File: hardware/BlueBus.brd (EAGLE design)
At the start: 70 x 45 mm, 77 parts

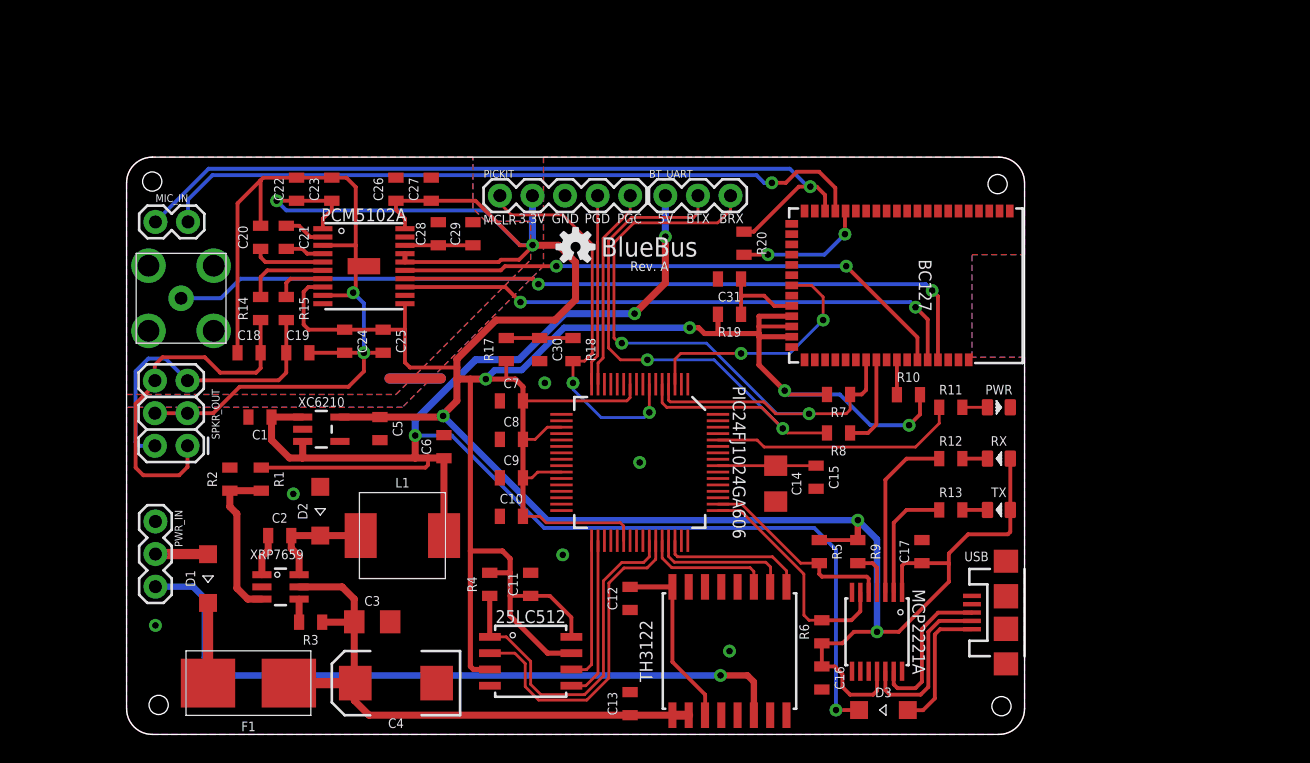
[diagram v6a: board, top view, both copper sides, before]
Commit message: [IMP] hardware: MIC IN Fixes
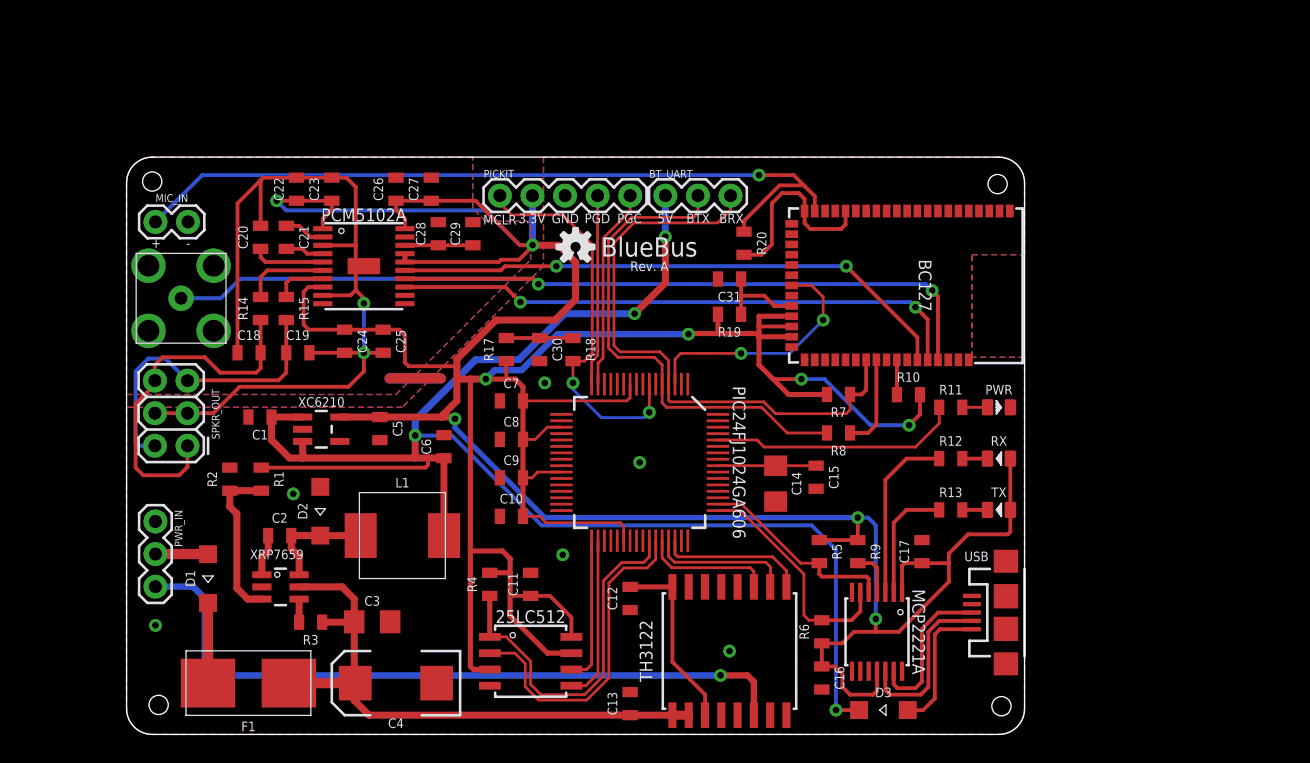
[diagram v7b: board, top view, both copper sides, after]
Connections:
- removed net BT_MIC_BIAS: BC127.17, R20.2
- removed net BT_MIC_RN: BC127.18, MIC_IN.2
- removed net BT_MIC_RP: BC127.19, MIC_IN.1, R20.1
- new net BT_MIC_IN: BC127.20, MIC_IN.1, R20.1
- new net MIC_BIAS: BC127.17, BC127.21, R20.2
- net 3.3V: no longer PCM5102A.11
- net GND: now also MIC_IN.2, PCM5102A.11
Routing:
- net BT_MIC_RP: track 62.6 -> 0.00 mm, vias 1 -> 0
- net BT_MIC_IN: track 0.00 -> 61.4 mm, vias 0 -> 1
- net BT_MIC_RN: track 55.9 -> 0.00 mm, vias 1 -> 0
- net MIC_BIAS: track 0.00 -> 15.3 mm
- net BT_MIC_BIAS: track 10.7 -> 0.00 mm, vias 2 -> 0
- net BT_UTX: track 57.2 -> 46.8 mm, vias 2 -> 0
- net BT_URX: track 56.4 -> 46.5 mm, vias 2 -> 0

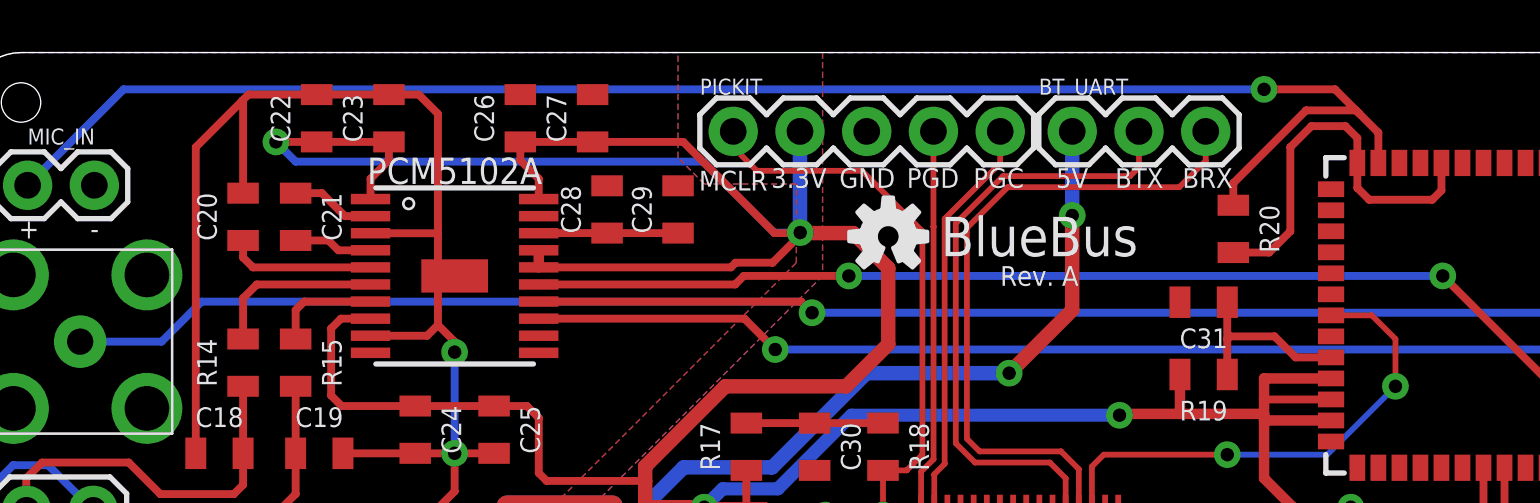
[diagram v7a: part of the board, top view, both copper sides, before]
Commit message: [IMP] hardware: Clean up traces * Clean up trace runs so we use less VIAs * Ensure that VIAs are not mid-trace on signal lines
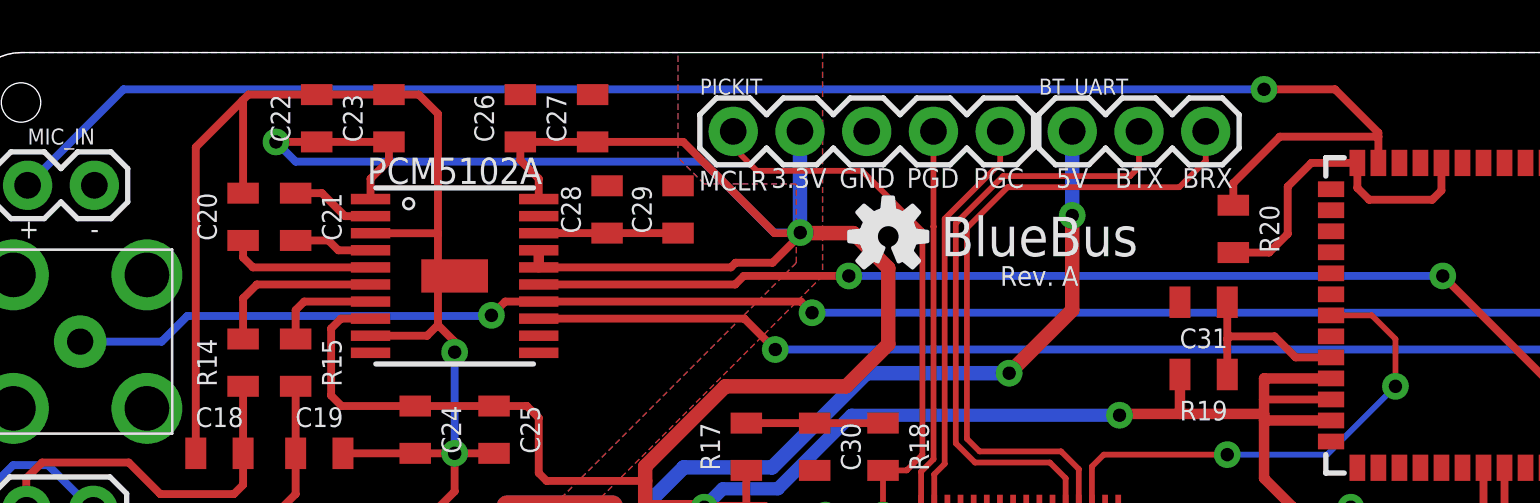
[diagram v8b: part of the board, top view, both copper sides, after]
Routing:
- net BT_DOUT: track 75.7 -> 65.2 mm, vias 2 -> 3
- net MIC_BIAS: track 15.3 -> 12.7 mm
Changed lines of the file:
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@@
 <wire x1="62.3" y1="35.1" x2="32.1" y2="35.1" width="0.3" layer="16"/>
 <wire x1="4.25" y1="34" x2="7.35" y2="34" width="0.3" layer="16"/>
-<wire x1="8.8732" y1="35.5232" x2="31.6768" y2="35.5232" width="0.3" layer="16"/>
-<wire x1="31.6768" y1="35.5232" x2="32.1" y2="35.1" width="0.3" layer="16"/>
-<wire x1="7.35" y1="34" x2="8.8732" y2="35.5232" width="0.3" layer="16"/>
+<wire x1="7.35" y1="34" x2="8.325" y2="34.975" width="0.3" layer="16"/>
 <contactref element="PCM5102A" pad="14"/>
 <wire x1="21.7" y1="35.525" x2="31.675" y2="35.525" width="0.3" layer="1"/>
 <wire x1="31.675" y1="35.525" x2="32.1" y2="35.1" width="0.3" layer="1"/>
+<wire x1="21.7" y1="35.525" x2="20.425" y2="35.525" width="0.3" layer="1"/>
+<wire x1="20.425" y1="35.525" x2="19.9" y2="35" width="0.3" layer="1"/>
+<via x="19.9" y="35" extent="1-16" drill="0.51"/>
+<wire x1="19.9" y1="35" x2="19.875" y2="34.975" width="0.3" layer="16"/>
+<wire x1="19.875" y1="34.975" x2="8.325" y2="34.975" width="0.3" layer="16"/>
 </signal>
 <signal name="BT_URX" class="5">
@@
 <contactref element="BC127" pad="21"/>
 <contactref element="R20" pad="2"/>
-<wire x1="52.85" y1="40.8" x2="52.85" y2="41.75" width="0.3" layer="1"/>
-<wire x1="52.4" y1="42.2" x2="51.1" y2="42.2" width="0.3" layer="1"/>
-<wire x1="51.1" y1="42.2" x2="50.3" y2="41.4" width="0.3" layer="1"/>
-<wire x1="50.3" y1="41.4" x2="50.3" y2="38.2" width="0.3" layer="1"/>
-<wire x1="50.3" y1="38.2" x2="49.49" y2="37.39" width="0.3" layer="1"/>
-<wire x1="49.49" y1="37.39" x2="48.13" y2="37.39" width="0.3" layer="1"/>
-<wire x1="52.85" y1="41.75" x2="52.4" y2="42.2" width="0.3" layer="1"/>
+<wire x1="48.13" y1="37.39" x2="49.49" y2="37.39" width="0.3" layer="1"/>
 <wire x1="52.85" y1="40.8" x2="52.85" y2="39.85" width="0.3" layer="1"/>
 <wire x1="53.3" y1="39.4" x2="52.85" y2="39.85" width="0.3" layer="1"/>
@@
 <wire x1="56.05" y1="39.75" x2="55.7" y2="39.4" width="0.3" layer="1"/>
 <wire x1="55.7" y1="39.4" x2="53.3" y2="39.4" width="0.3" layer="1"/>
+<wire x1="52.85" y1="40.8" x2="51.1" y2="40.8" width="0.3" layer="1"/>
+<wire x1="51.1" y1="40.8" x2="50.2" y2="39.9" width="0.3" layer="1"/>
+<wire x1="50.2" y1="38.1" x2="49.49" y2="37.39" width="0.3" layer="1"/>
+<wire x1="50.2" y1="39.9" x2="50.2" y2="38.1" width="0.3" layer="1"/>
 </signal>
 <signal name="BT_MIC_IN">
@@
 <wire x1="5.9" y1="43.6" x2="49.3" y2="43.6" width="0.3" layer="16"/>
 <contactref element="R20" pad="1"/>
-<wire x1="48.13" y1="40.03" x2="48.13" y2="39.19" width="0.3" layer="1"/>
-<wire x1="53.65" y1="40.8" x2="53.65" y2="41.95" width="0.3" layer="1"/>
-<wire x1="53.65" y1="41.95" x2="52.9" y2="42.7" width="0.3" layer="1"/>
-<wire x1="52.9" y1="42.7" x2="52.8" y2="42.8" width="0.3" layer="1"/>
-<wire x1="52.8" y1="42.8" x2="50.9" y2="42.8" width="0.3" layer="1"/>
-<wire x1="50.9" y1="42.8" x2="48.13" y2="40.03" width="0.3" layer="1"/>
+<wire x1="48.13" y1="39.19" x2="48.13" y2="40.03" width="0.3" layer="1"/>
+<wire x1="53.65" y1="40.8" x2="53.65" y2="41.8" width="0.3" layer="1"/>
 <via x="49.3" y="43.6" extent="1-16" drill="0.51"/>
-<wire x1="52" y1="43.6" x2="52.8" y2="42.8" width="0.3" layer="1"/>
+<wire x1="53.65" y1="41.8" x2="53.65" y2="41.95" width="0.3" layer="1"/>
+<wire x1="52" y1="43.6" x2="53.65" y2="41.95" width="0.3" layer="1"/>
 <wire x1="49.3" y1="43.6" x2="52" y2="43.6" width="0.3" layer="1"/>
+<wire x1="48.13" y1="40.03" x2="49.9" y2="41.8" width="0.3" layer="1"/>
+<wire x1="49.9" y1="41.8" x2="53.65" y2="41.8" width="0.3" layer="1"/>
 </signal>
 </signals>
